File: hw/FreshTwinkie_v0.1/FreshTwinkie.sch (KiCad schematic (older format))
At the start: 54 parts, among them J1 USB_C_Receptacle, J2 USB_B_Micro, P1 USB_C_Plug, Q1 BSD840NH6327XTSA1, Q2 BSD840NH6327XTSA1, Q3 BSD840NH6327XTSA1, Q4 BSD840NH6327XTSA1, SW1 SW_Push, U1 AD8606ARMZ-REEL, U2 STM32F072CBUx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

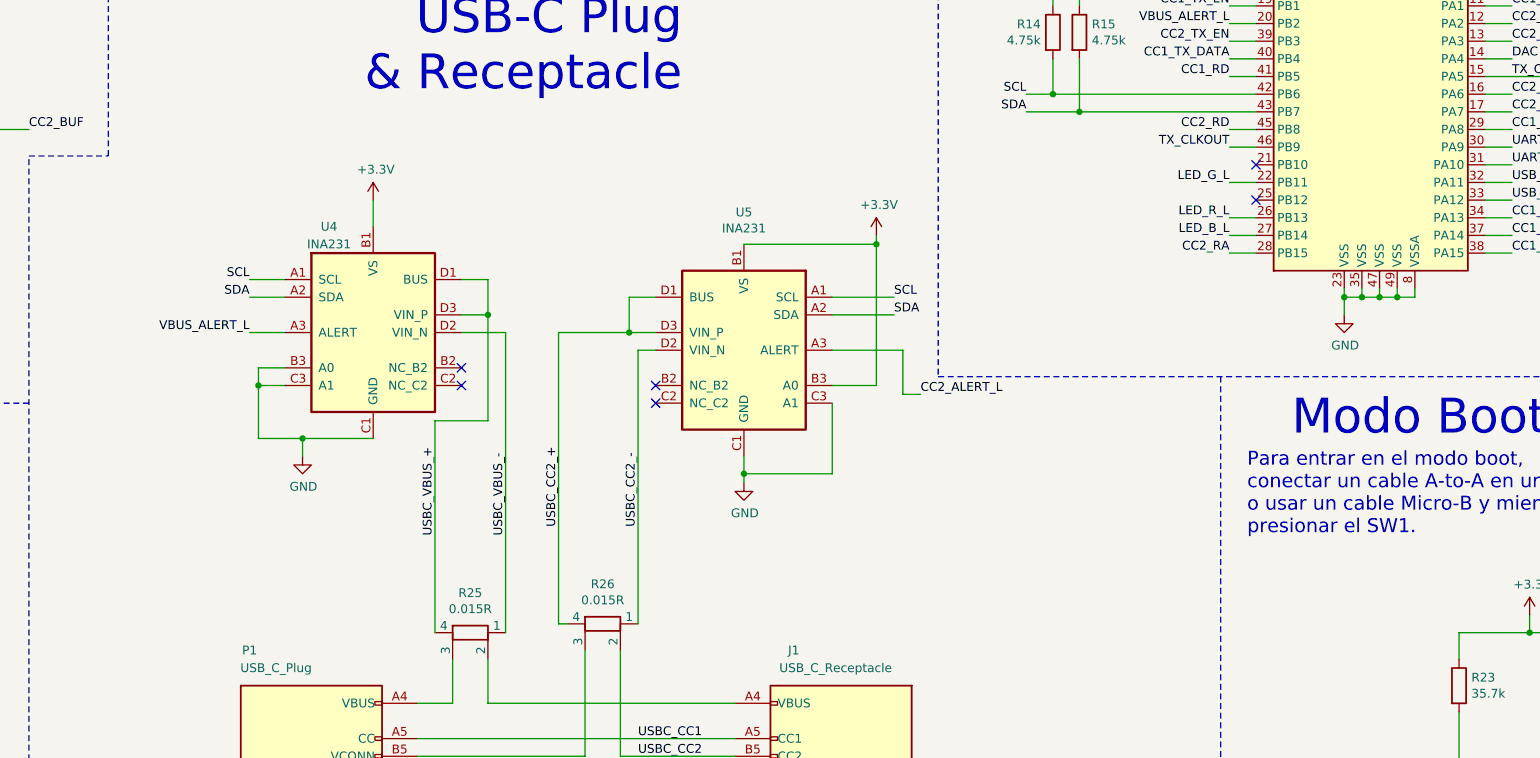
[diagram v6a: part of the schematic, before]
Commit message: changeINA231forINA226
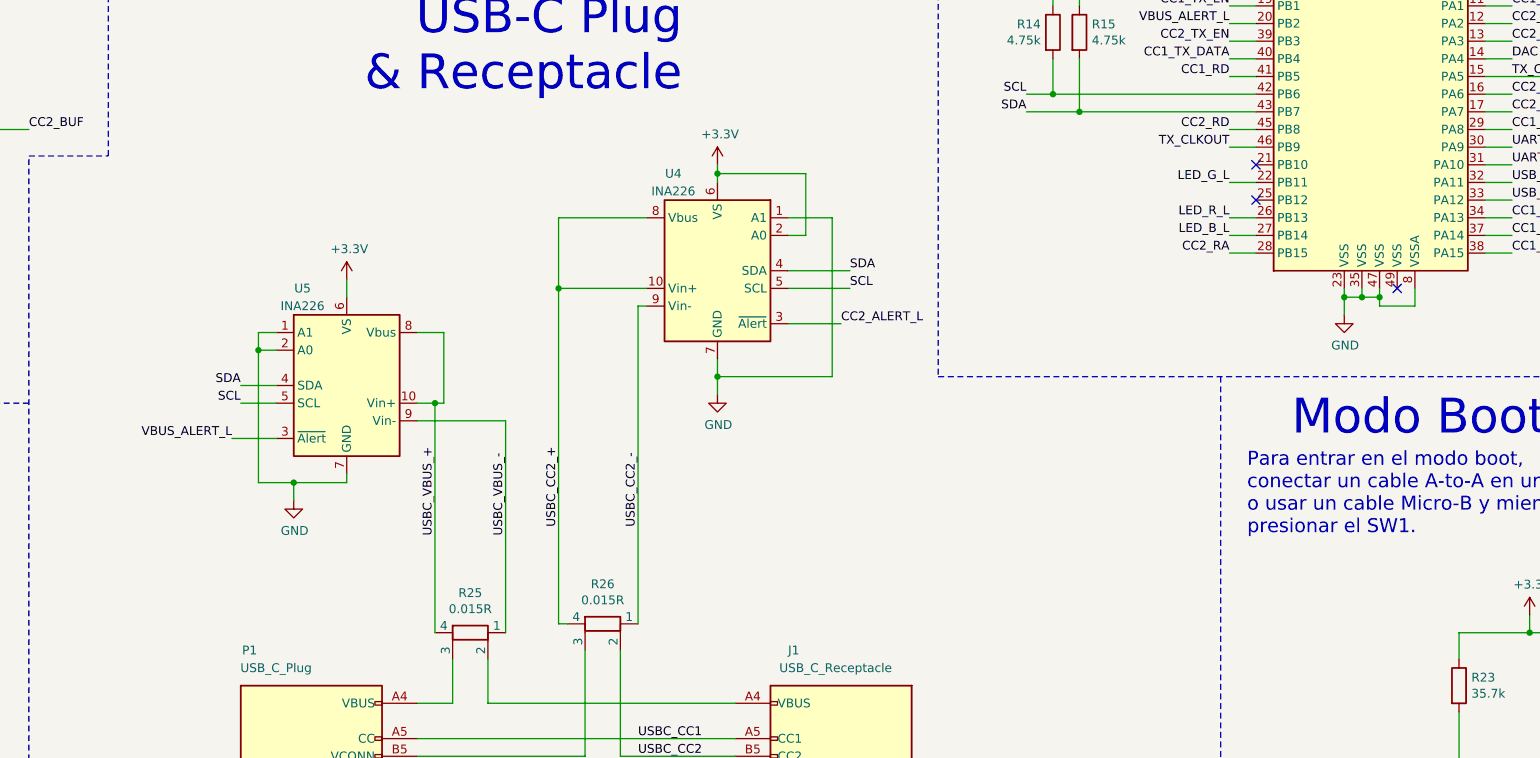
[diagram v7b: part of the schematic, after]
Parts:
- removed U4, U5: INA231, BGA12N40P3X4_119X159X62N:BGA12N40P3X4_119X159X62N, symbol gkl_sensor:INA231
- added U4, U5: INA226, Package_SO:VSSOP-10_3x3mm_P0.5mm, symbol Analog_ADC:INA226
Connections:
- net +3V3: now also U4.2 (A0), U4.6 (VS), U5.6 (VS)
- net CC2_ALERT_L: now also U4.3 (~Alert~)
- net GND: now also U4.1 (A1), U4.7 (GND), U5.1 (A1), U5.2 (A0), U5.7 (GND); no longer U2.49 (VSS)
- net SCL: now also U4.5 (SCL), U5.5 (SCL)
- net SDA: now also U4.4 (SDA), U5.4 (SDA)
- net USBC_CC2_+: now also U4.10 (Vin+), U4.8 (Vbus)
- net USBC_CC2_-: now also U4.9 (Vin-)
- net USBC_VBUS_+: now also U5.10 (Vin+), U5.8 (Vbus)
- net USBC_VBUS_-: now also U5.9 (Vin-)
- net VBUS_ALERT_L: now also U5.3 (~Alert~)
- no-connect marks 9 -> 6
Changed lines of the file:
@@
 Connection ~ 13600 5750
-Wire Wire Line
-	13800 5700 13800 5750
-Wire Wire Line
-	13800 5750 13700 5750
-Connection ~ 13700 5750
-Wire Wire Line
-	13900 5700 13900 5750
-Wire Wire Line
-	13900 5750 13800 5750
-Connection ~ 13800 5750
 Wire Wire Line
 	14300 4000 14450 4000
@@
 	1    0    0    -1
 $EndComp
-Text Label 7300 5950 2    50   ~ 0
-VBUS_ALERT_L
-Text Label 7300 5750 2    50   ~ 0
-SDA
 Wire Notes Line
 	8000 500  8000 3450
@@
 	0    1    1    0
 $EndComp
-$Comp
-L power:GND #PWR024
-U 1 1 604F7F22
-P 7600 6650
-F 0 "#PWR024" H 7600 6400 50  0001 C CNN
-F 1 "GND" H 7605 6477 50  0000 C CNN
-F 2 "" H 7600 6650 50  0001 C CNN
-F 3 "" H 7600 6650 50  0001 C CNN
-	1    7600 6650
-	1    0    0    -1
-$EndComp
-$Comp
-L power:GND #PWR026
-U 1 1 6050FCBB
-P 10100 6800
-F 0 "#PWR026" H 10100 6550 50  0001 C CNN
-F 1 "GND" H 10105 6627 50  0000 C CNN
-F 2 "" H 10100 6800 50  0001 C CNN
-F 3 "" H 10100 6800 50  0001 C CNN
-	1    10100 6800
-	1    0    0    -1
-$EndComp
-$Comp
-L power:+3.3V #PWR021
-U 1 1 605F6E31
-P 8000 5200
-F 0 "#PWR021" H 8000 5050 50  0001 C CNN
-F 1 "+3.3V" H 8015 5373 50  0000 C CNN
-F 2 "" H 8000 5200 50  0001 C CNN
-F 3 "" H 8000 5200 50  0001 C CNN
-	1    8000 5200
-	1    0    0    -1
-$EndComp
-$Comp
-L power:+3.3V #PWR022
-U 1 1 60656CD3
-P 10850 5400
-F 0 "#PWR022" H 10850 5250 50  0001 C CNN
-F 1 "+3.3V" H 10865 5573 50  0000 C CNN
-F 2 "" H 10850 5400 50  0001 C CNN
-F 3 "" H 10850 5400 50  0001 C CNN
-	1    10850 5400
-	1    0    0    -1
-$EndComp
-Wire Wire Line
-	10850 5400 10850 5450
-Wire Wire Line
-	10850 6250 10600 6250
-Wire Wire Line
-	10100 5450 10850 5450
-Connection ~ 10850 5450
-Wire Wire Line
-	10850 5450 10850 6250
 Wire Wire Line
 	7350 10650 7350 10700
@@
 	7500 10700 7650 10700
 Wire Wire Line
-	9450 5950 9600 5950
-Wire Wire Line
-	9600 5750 9450 5750
-Wire Wire Line
-	9450 5750 9450 5950
-Wire Wire Line
 	8250 8050 8450 8050
 Wire Wire Line
@@
 Wire Wire Line
 	9400 8350 9400 7750
-Text Label 7300 5650 2    50   ~ 0
-SCL
-Wire Wire Line
-	8000 5350 8000 5200
-Wire Wire Line
-	7300 5750 7500 5750
-Wire Wire Line
-	7300 5650 7500 5650
 Wire Notes Line
 	5750 11200 6050 11200
@@
 Wire Notes Line
 	500  6350 500  6300
-Wire Wire Line
-	7300 5950 7500 5950
-$Comp
-L gkl_sensor:INA231 U4
-U 1 1 604C232E
-P 8000 5900
-F 0 "U4" H 7750 6450 50  0000 C CNN
-F 1 "INA231" H 7750 6350 50  0000 C CNN
-F 2 "BGA12N40P3X4_119X159X62N:BGA12N40P3X4_119X159X62N" H 8000 6600 50  0001 C CNN
-F 3 "https://www.ti.com/general/docs/suppproductinfo.tsp?distId=26&gotoUrl=http%3A%2F%2Fwww.ti.com%2Flit%2Fgpn%2Fina231" H 8000 6600 50  0001 C CNN
-F 4 "Texas Instruments" H 8000 5900 50  0001 C CNN "Mfg"
-F 5 "595-INA231AIYFFR" H 8000 5900 50  0001 C CNN "PN"
-F 6 "Mouser" H 8000 5900 50  0001 C CNN "Tienda"
-	1    8000 5900
-	1    0    0    -1
-$EndComp
-Wire Wire Line
-	8000 6550 7600 6550
-Wire Wire Line
-	7600 6550 7600 6650
-Wire Wire Line
-	7500 6150 7350 6150
-Wire Wire Line
-	7350 6150 7350 6250
-Wire Wire Line
-	7350 6250 7500 6250
-Wire Wire Line
-	7350 6250 7350 6550
-Wire Wire Line
-	7350 6550 7600 6550
-Connection ~ 7350 6250
-Connection ~ 7600 6550
-NoConn ~ 8500 6250
-NoConn ~ 8500 6150
-Wire Wire Line
-	8350 7650 8350 6450
-Wire Wire Line
-	8350 6450 8650 6450
-Wire Wire Line
-	8650 6450 8650 5850
-Wire Wire Line
-	8650 5850 8500 5850
-Wire Wire Line
-	8500 5650 8650 5650
-Wire Wire Line
-	8650 5650 8650 5850
-Connection ~ 8650 5850
-Wire Wire Line
-	8750 7650 8750 5950
-Wire Wire Line
-	8750 5950 8500 5950
-$Comp
-L gkl_sensor:INA231 U5
-U 1 1 604C3169
-P 10100 6000
-F 0 "U5" H 10100 6731 50  0000 C CNN
-F 1 "INA231" H 10100 6640 50  0000 C CNN
-F 2 "BGA12N40P3X4_119X159X62N:BGA12N40P3X4_119X159X62N" H 10100 6700 50  0001 C CNN
-F 3 "https://www.ti.com/general/docs/suppproductinfo.tsp?distId=26&gotoUrl=http%3A%2F%2Fwww.ti.com%2Flit%2Fgpn%2Fina231" H 10100 6700 50  0001 C CNN
-F 4 "Texas Instruments" H 10100 6000 50  0001 C CNN "Mfg"
-F 5 "595-INA231AIYFFR" H 10100 6000 50  0001 C CNN "PN"
-F 6 "Mouser" H 10100 6000 50  0001 C CNN "Tienda"
-	1    10100 6000
-	-1   0    0    -1
-$EndComp
-Wire Wire Line
-	9050 7600 9050 5950
-Wire Wire Line
-	9050 5950 9450 5950
-Connection ~ 9450 5950
-Wire Wire Line
-	9500 7600 9500 6050
-Wire Wire Line
-	9500 6050 9600 6050
-Wire Wire Line
-	10100 6800 10100 6750
-Wire Wire Line
-	10600 6350 10600 6750
-Wire Wire Line
-	10600 6750 10100 6750
-Connection ~ 10100 6750
-Wire Wire Line
-	10100 6750 10100 6650
-Text Label 10950 5750 0    50   ~ 0
+Text Label 10700 5700 0    50   ~ 0
 SCL
-Text Label 10950 5850 0    50   ~ 0
+Text Label 10700 5600 0    50   ~ 0
 SDA
-Wire Wire Line
-	10600 5750 10950 5750
-Wire Wire Line
-	10600 5850 10950 5850
-Text Label 11100 6300 0    50   ~ 0
+Text Label 10650 5900 0    50   ~ 0
 CC2_ALERT_L
-Wire Wire Line
-	10600 6050 11000 6050
-Wire Wire Line
-	11000 6050 11000 6300
-Wire Wire Line
-	11000 6300 11100 6300
-NoConn ~ 9600 6250
-NoConn ~ 9600 6350
 Text Label 8350 7100 1    50   ~ 0
 USBC_VBUS_+
@@
 Wire Wire Line
 	3700 10200 3700 10350
+$Comp
+L Analog_ADC:INA226 U5
+U 1 1 606DC2B7
+P 7850 6250
+F 0 "U5" H 8100 6800 50  0000 C CNN
+F 1 "INA226" H 8100 6700 50  0000 C CNN
+F 2 "Package_SO:VSSOP-10_3x3mm_P0.5mm" H 8650 5800 50  0001 C CNN
+F 3 "http://www.ti.com/lit/ds/symlink/ina226.pdf" H 8200 6150 50  0001 C CNN
+F 4 "Texas Instruments" H 7850 6250 50  0001 C CNN "Mfg"
+F 5 "595-INA226AIDGSR " H 7850 6250 50  0001 C CNN "PN"
+F 6 "Mouser" H 7850 6250 50  0001 C CNN "Tienda"
+	1    7850 6250
+	-1   0    0    -1
+$EndComp
+Text Label 7200 6550 2    50   ~ 0
+VBUS_ALERT_L
+Wire Wire Line
+	7200 6550 7450 6550
+Text Label 7250 6250 2    50   ~ 0
+SDA
+Wire Wire Line
+	7250 6250 7450 6250
+Text Label 7250 6350 2    50   ~ 0
+SCL
+Wire Wire Line
+	7250 6350 7450 6350
+Wire Wire Line
+	7450 5950 7350 5950
+Wire Wire Line
+	7350 5950 7350 6050
+Wire Wire Line
+	7350 6800 7550 6800
+Wire Wire Line
+	7850 6800 7850 6750
+Wire Wire Line
+	7450 6050 7350 6050
+Connection ~ 7350 6050
+Wire Wire Line
+	7350 6050 7350 6800
+$Comp
+L power:GND #PWR026
+U 1 1 6079C960
+P 7550 6900
+F 0 "#PWR026" H 7550 6650 50  0001 C CNN
+F 1 "GND" H 7555 6727 50  0000 C CNN
+F 2 "" H 7550 6900 50  0001 C CNN
+F 3 "" H 7550 6900 50  0001 C CNN
+	1    7550 6900
+	1    0    0    -1
+$EndComp
+Wire Wire Line
+	7550 6900 7550 6800
+Connection ~ 7550 6800
+Wire Wire Line
+	7550 6800 7850 6800
+$Comp
+L power:+3.3V #PWR022
+U 1 1 607BE22F
+P 7850 5650
+F 0 "#PWR022" H 7850 5500 50  0001 C CNN
+F 1 "+3.3V" H 7865 5823 50  0000 C CNN
+F 2 "" H 7850 5650 50  0001 C CNN
+F 3 "" H 7850 5650 50  0001 C CNN
+	1    7850 5650
+	1    0    0    -1
+$EndComp
+Wire Wire Line
+	7850 5650 7850 5750
+Wire Wire Line
+	8250 5950 8400 5950
+Wire Wire Line
+	8400 5950 8400 6350
+Wire Wire Line
+	8400 6350 8350 6350
+Wire Wire Line
+	8350 6350 8350 7650
+Connection ~ 8350 6350
+Wire Wire Line
+	8350 6350 8250 6350
+Wire Wire Line
+	8750 6450 8250 6450
+Wire Wire Line
+	8750 6450 8750 7650
+$Comp
+L Analog_ADC:INA226 U4
+U 1 1 6099B7C9
+P 9950 5600
+F 0 "U4" H 9700 6150 50  0000 C CNN
+F 1 "INA226" H 9700 6050 50  0000 C CNN
+F 2 "Package_SO:VSSOP-10_3x3mm_P0.5mm" H 10750 5150 50  0001 C CNN
+F 3 "http://www.ti.com/lit/ds/symlink/ina226.pdf" H 10300 5500 50  0001 C CNN
+F 4 "Texas Instruments" H 9950 5600 50  0001 C CNN "Mfg"
+F 5 "595-INA226AIDGSR " H 9950 5600 50  0001 C CNN "PN"
+F 6 "Mouser" H 9950 5600 50  0001 C CNN "Tienda"
+	1    9950 5600
+	1    0    0    -1
+$EndComp
+$Comp
+L power:GND #PWR024
+U 1 1 609F9D36
+P 9950 6300
+F 0 "#PWR024" H 9950 6050 50  0001 C CNN
+F 1 "GND" H 9955 6127 50  0000 C CNN
+F 2 "" H 9950 6300 50  0001 C CNN
+F 3 "" H 9950 6300 50  0001 C CNN
+	1    9950 6300
+	1    0    0    -1
+$EndComp
+Wire Wire Line
+	9950 6300 9950 6200
+Wire Wire Line
+	10350 5300 10600 5300
+Wire Wire Line
+	10600 5300 10600 6200
+Wire Wire Line
+	10600 6200 9950 6200
+Connection ~ 9950 6200
+Wire Wire Line
+	9950 6200 9950 6100
+$Comp
+L power:+3.3V #PWR021
+U 1 1 60A3A1AF
+P 9950 5000
+F 0 "#PWR021" H 9950 4850 50  0001 C CNN
+F 1 "+3.3V" H 9965 5173 50  0000 C CNN
+F 2 "" H 9950 5000 50  0001 C CNN
+F 3 "" H 9950 5000 50  0001 C CNN
+	1    9950 5000
+	1    0    0    -1
+$EndComp
+Wire Wire Line
+	9950 5000 9950 5050
+Wire Wire Line
+	10350 5400 10450 5400
+Wire Wire Line
+	10450 5400 10450 5050
+Wire Wire Line
+	10450 5050 9950 5050
+Connection ~ 9950 5050
+Wire Wire Line
+	9950 5050 9950 5100
+Wire Wire Line
+	10700 5600 10350 5600
+Wire Wire Line
+	10700 5700 10350 5700
+Wire Wire Line
+	10650 5900 10350 5900
+Wire Wire Line
+	9500 5800 9550 5800
+Wire Wire Line
+	9500 5800 9500 7600
+Wire Wire Line
+	9050 5300 9550 5300
+Wire Wire Line
+	9050 5300 9050 5700
+Wire Wire Line
+	9550 5700 9050 5700
+Connection ~ 9050 5700
+Wire Wire Line
+	9050 5700 9050 7600
+NoConn ~ 13800 5700
+Wire Wire Line
+	13900 5800 13700 5800
+Wire Wire Line
+	13700 5800 13700 5750
+Wire Wire Line
+	13900 5700 13900 5800
+Connection ~ 13700 5750
 $EndSCHEMATC

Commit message: changeUSB-CReceptacle
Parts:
- J1: footprint Footprint:XUNPU_24PIN_USBC_RECEPT -> Connector_USB:USB_C_Receptacle_Amphenol_12401610E4-2A; Mfg XUNPU -> 12401610E4#2A; PN C920230 -> 523-12401610E4#2A; Tienda LCSC -> Mouser
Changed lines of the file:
@@
 F 0 "J1" H 10950 10350 50  0000 R CNN
 F 1 "USB_C_Receptacle" H 11000 10250 50  0000 R CNN
-F 2 "Footprint:XUNPU_24PIN_USBC_RECEPT" H 10800 9050 50  0001 C CNN
-F 3 "https://datasheet.lcsc.com/szlcsc/2012251035_XUNPU-TYPEC-324G-BCP24_C920230.pdf" H 10800 9050 50  0001 C CNN
-F 4 "C920230" H 10650 9050 50  0001 C CNN "PN"
-F 5 "XUNPU" H 10650 9050 50  0001 C CNN "Mfg"
-F 6 "LCSC" H 10650 9050 50  0001 C CNN "Tienda"
+F 2 "Connector_USB:USB_C_Receptacle_Amphenol_12401610E4-2A" H 10800 9050 50  0001 C CNN
+F 3 "https://www.usb.org/sites/default/files/documents/usb_type-c.zip" H 10800 9050 50  0001 C CNN
+F 4 "523-12401610E4#2A " H 10650 9050 50  0001 C CNN "PN"
+F 5 "12401610E4#2A" H 10650 9050 50  0001 C CNN "Mfg"
+F 6 "Mouser" H 10650 9050 50  0001 C CNN "Tienda"
 	1    10650 9050
 	-1   0    0    -1
